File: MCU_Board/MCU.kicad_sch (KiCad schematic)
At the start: 34 parts, among them SW1 SW_SPDT, SW2 SW_Push, U2 STM32L433CCTx, Y1 8MHz, Y2 32kHz

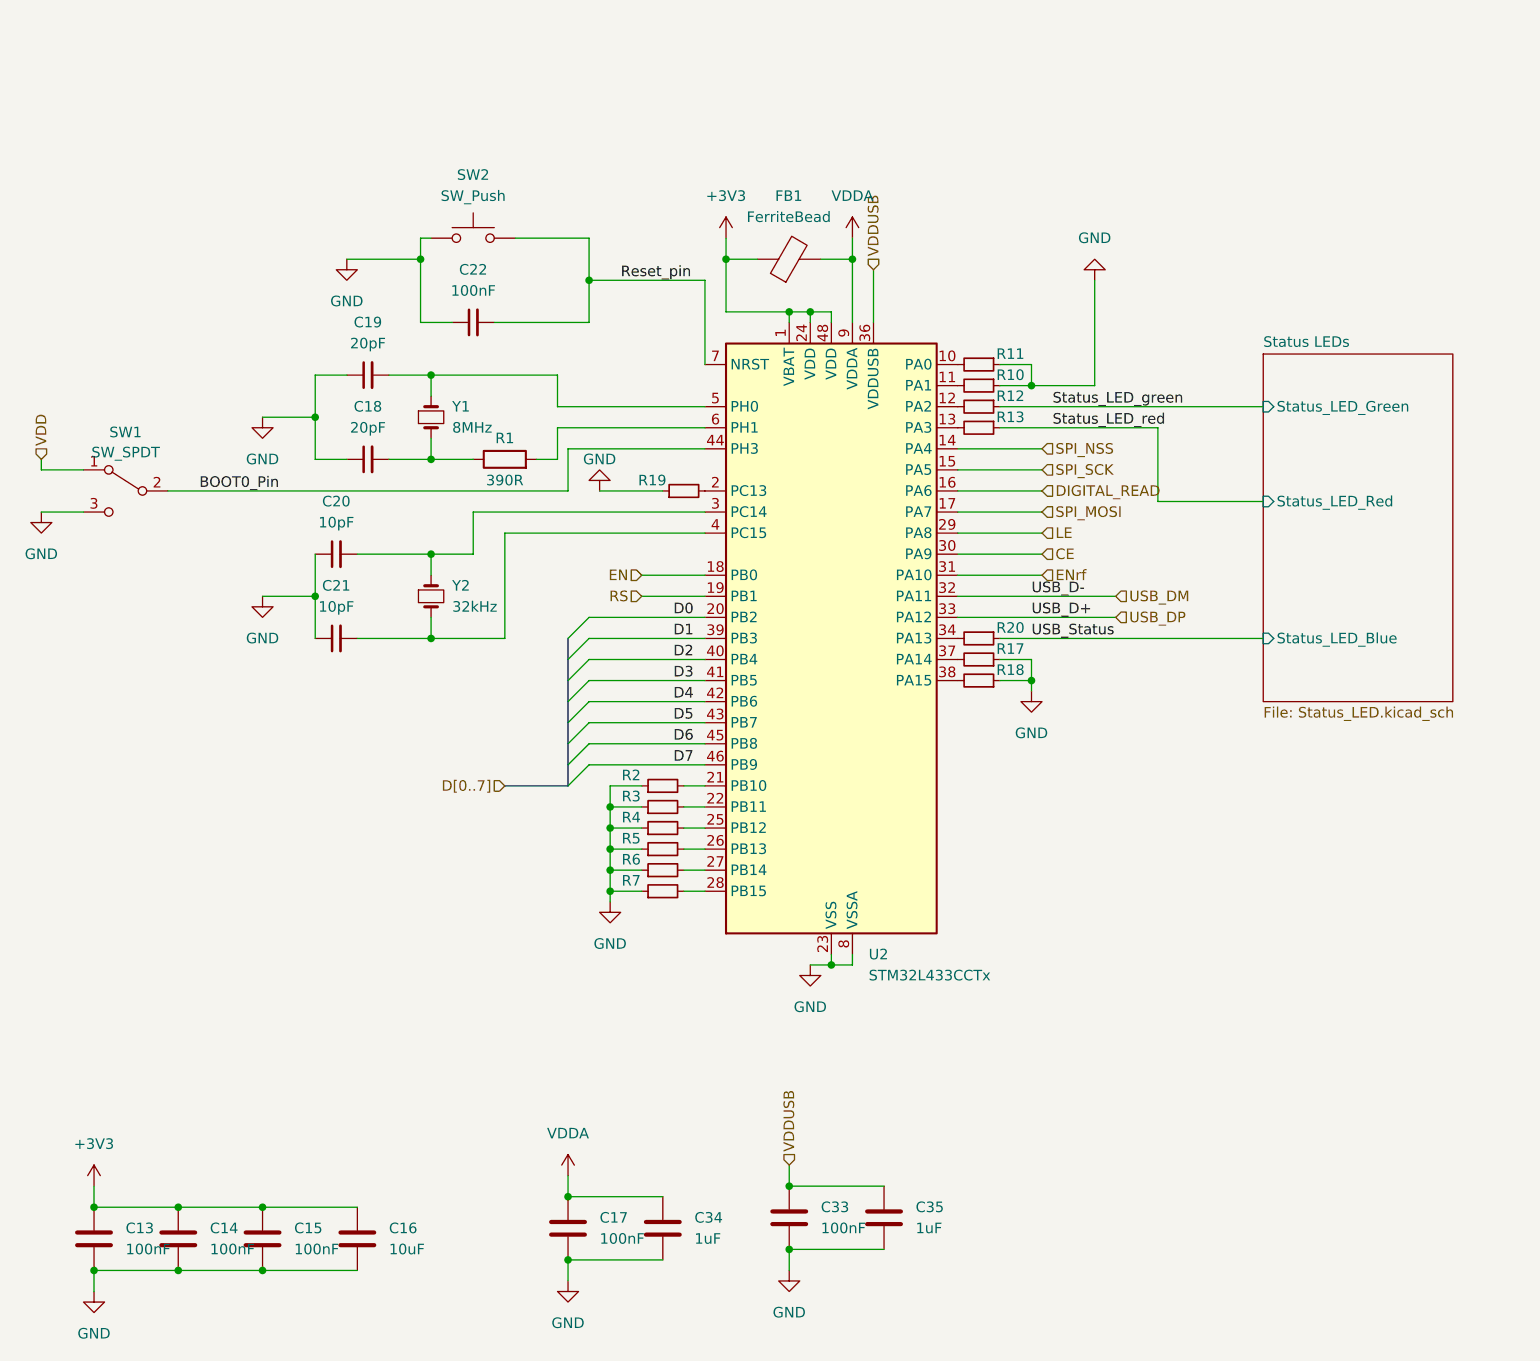
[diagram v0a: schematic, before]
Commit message: Added JTAG connector to MCU board
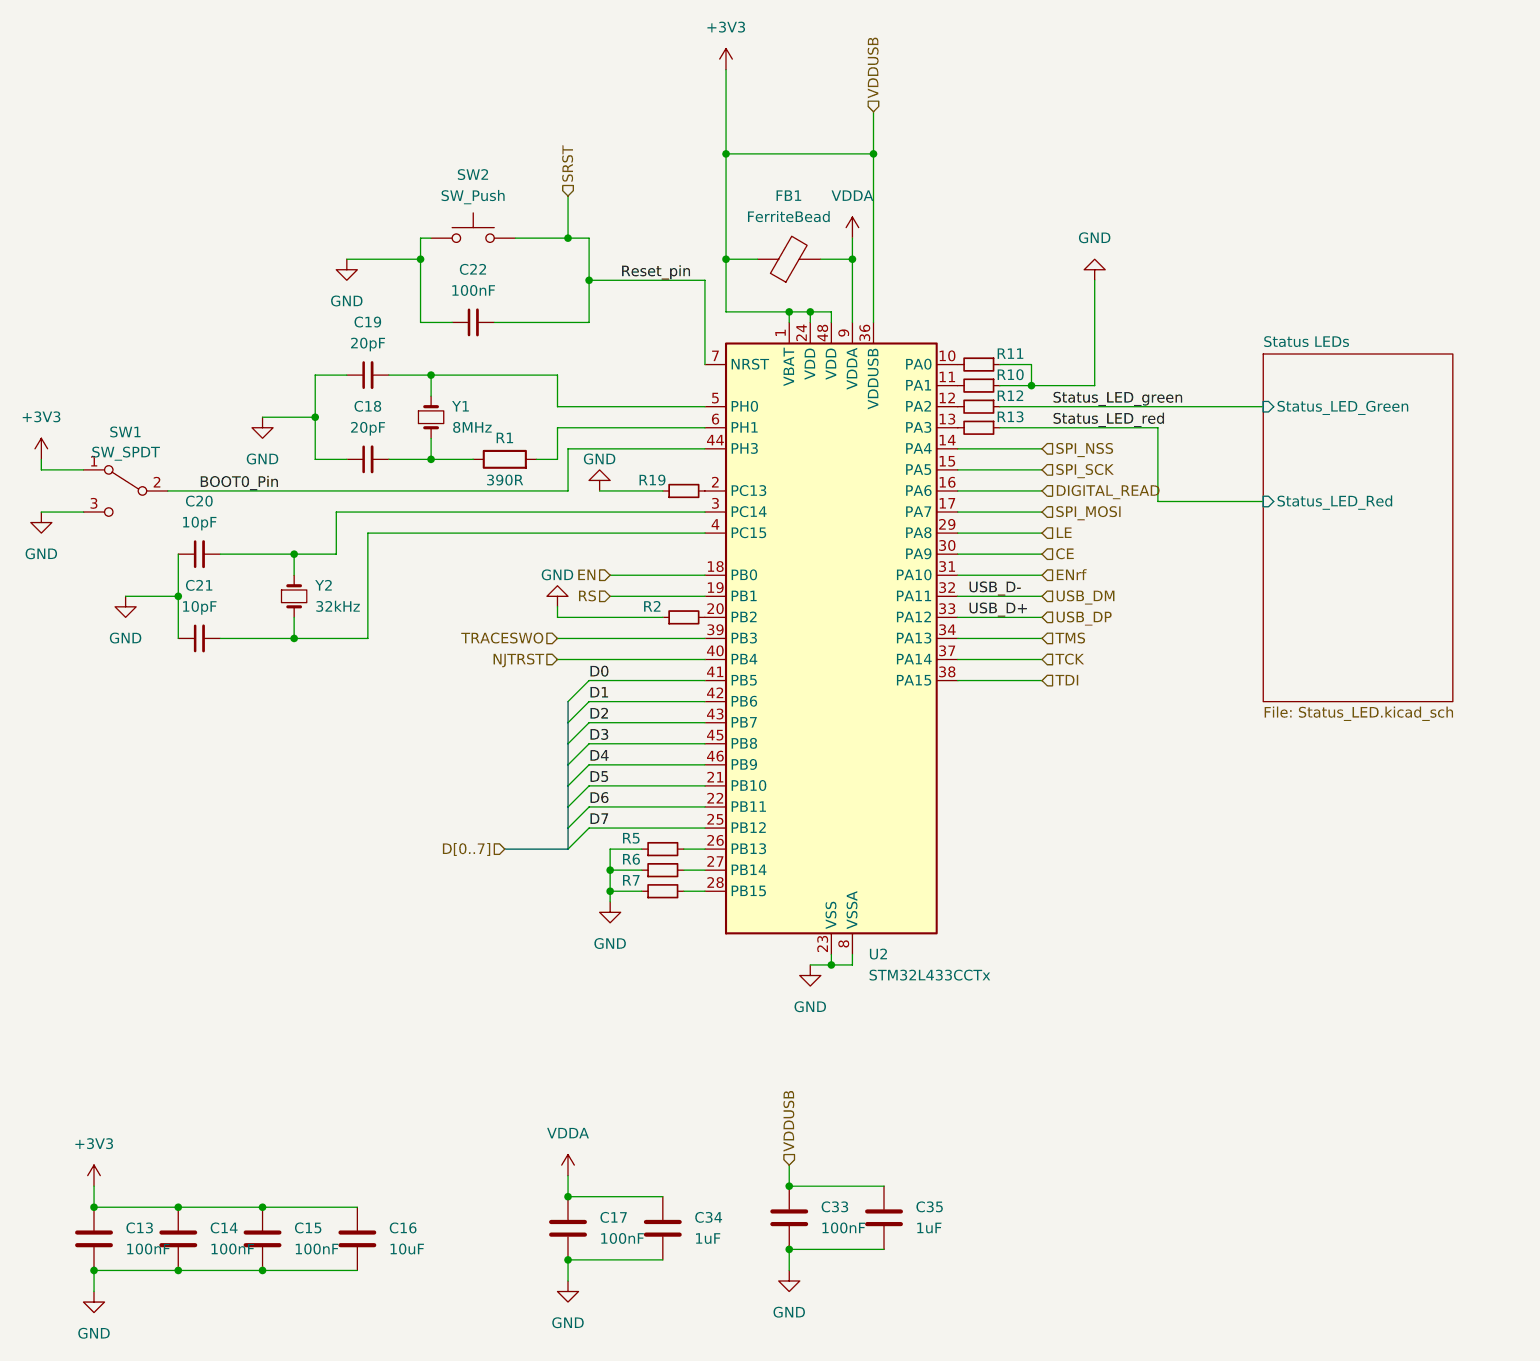
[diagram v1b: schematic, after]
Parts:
- removed R17, R18, R20, R3, R4: 10k, Resistor_SMD:R_0603_1608Metric_Pad0.98x0.95mm_HandSolder, symbol Device:R_Small
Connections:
- net VDD is gone; now on net +3V3: SW1.1 (A)
- net VDDUSB is gone; now on net +3V3: C33.1, C35.1, U2.36 (VDDUSB)
- net D0: now also U2.41 (PB5); no longer U2.20 (PB2)
- net D1: now also U2.42 (PB6); no longer U2.39 (PB3)
- net D2: now also U2.43 (PB7); no longer U2.40 (PB4)
- net D3: now also U2.45 (PB8); no longer U2.41 (PB5)
- net D4: now also U2.46 (PB9); no longer U2.42 (PB6)
- net D5: now also U2.21 (PB10); no longer U2.43 (PB7)
- net D6: now also U2.22 (PB11); no longer U2.45 (PB8)
- net D7: now also U2.25 (PB12); no longer U2.46 (PB9)
- net TMS: now reaches U2.34 (PA13)
- net TCK: now reaches U2.37 (PA14)
- net at R2.2: now also U2.20 (PB2); no longer U2.21 (PB10)
- net TDI: now reaches U2.38 (PA15)
- net Reset_pin renamed SRST
- new net NJTRST: U2.40 (PB4)
- new net TRACESWO: U2.39 (PB3)
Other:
- sheet Status LEDs ports: added none; removed Status_LED_Blue
- moved on the sheet: C20, C21, Y2

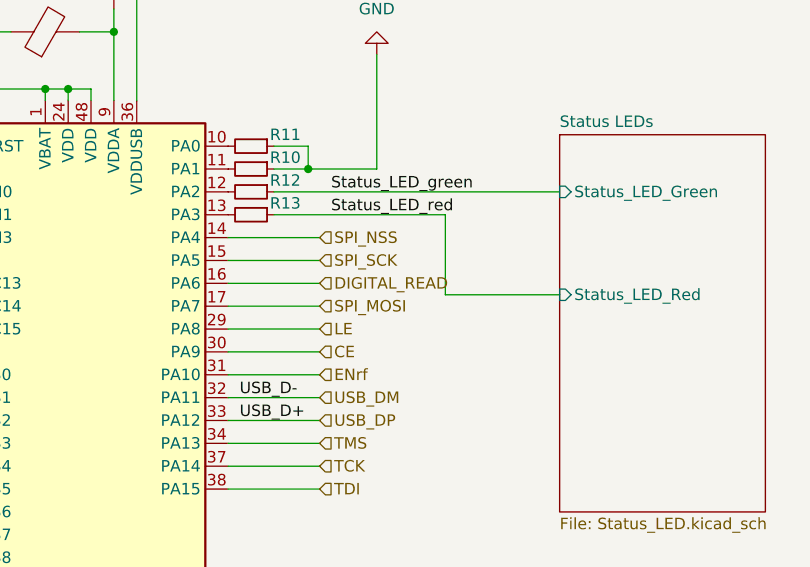
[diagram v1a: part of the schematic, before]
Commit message: Added a header for the VCO controls
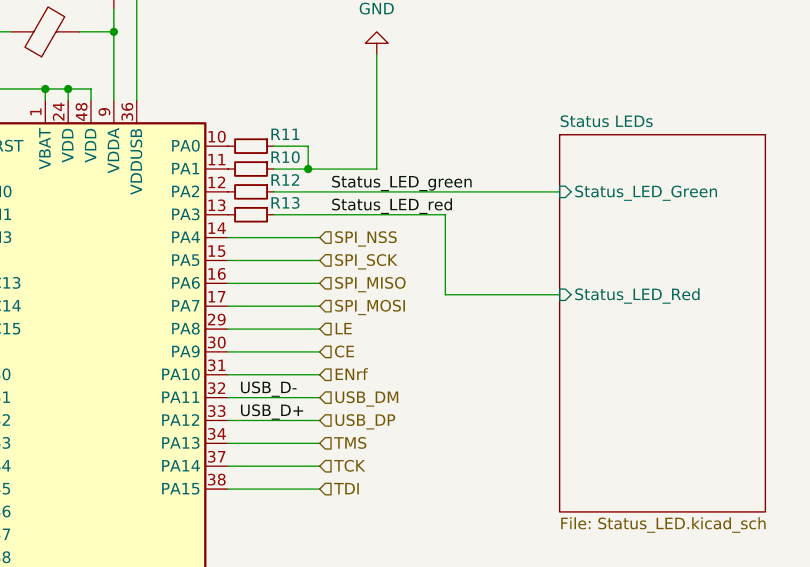
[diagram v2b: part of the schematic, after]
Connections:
- net DIGITAL_READ renamed SPI_MISO
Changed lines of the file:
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@@
     (effects (font (size 1.27 1.27)) (justify left bottom))
   )
-  (hierarchical_label "DIGITAL_READ" (shape input) (at 144.78 78.74 0) (fields_autoplaced)
+  (hierarchical_label "SPI_MISO" (shape input) (at 144.78 78.74 0) (fields_autoplaced)
     (effects (font (size 1.27 1.27)) (justify left))
   )

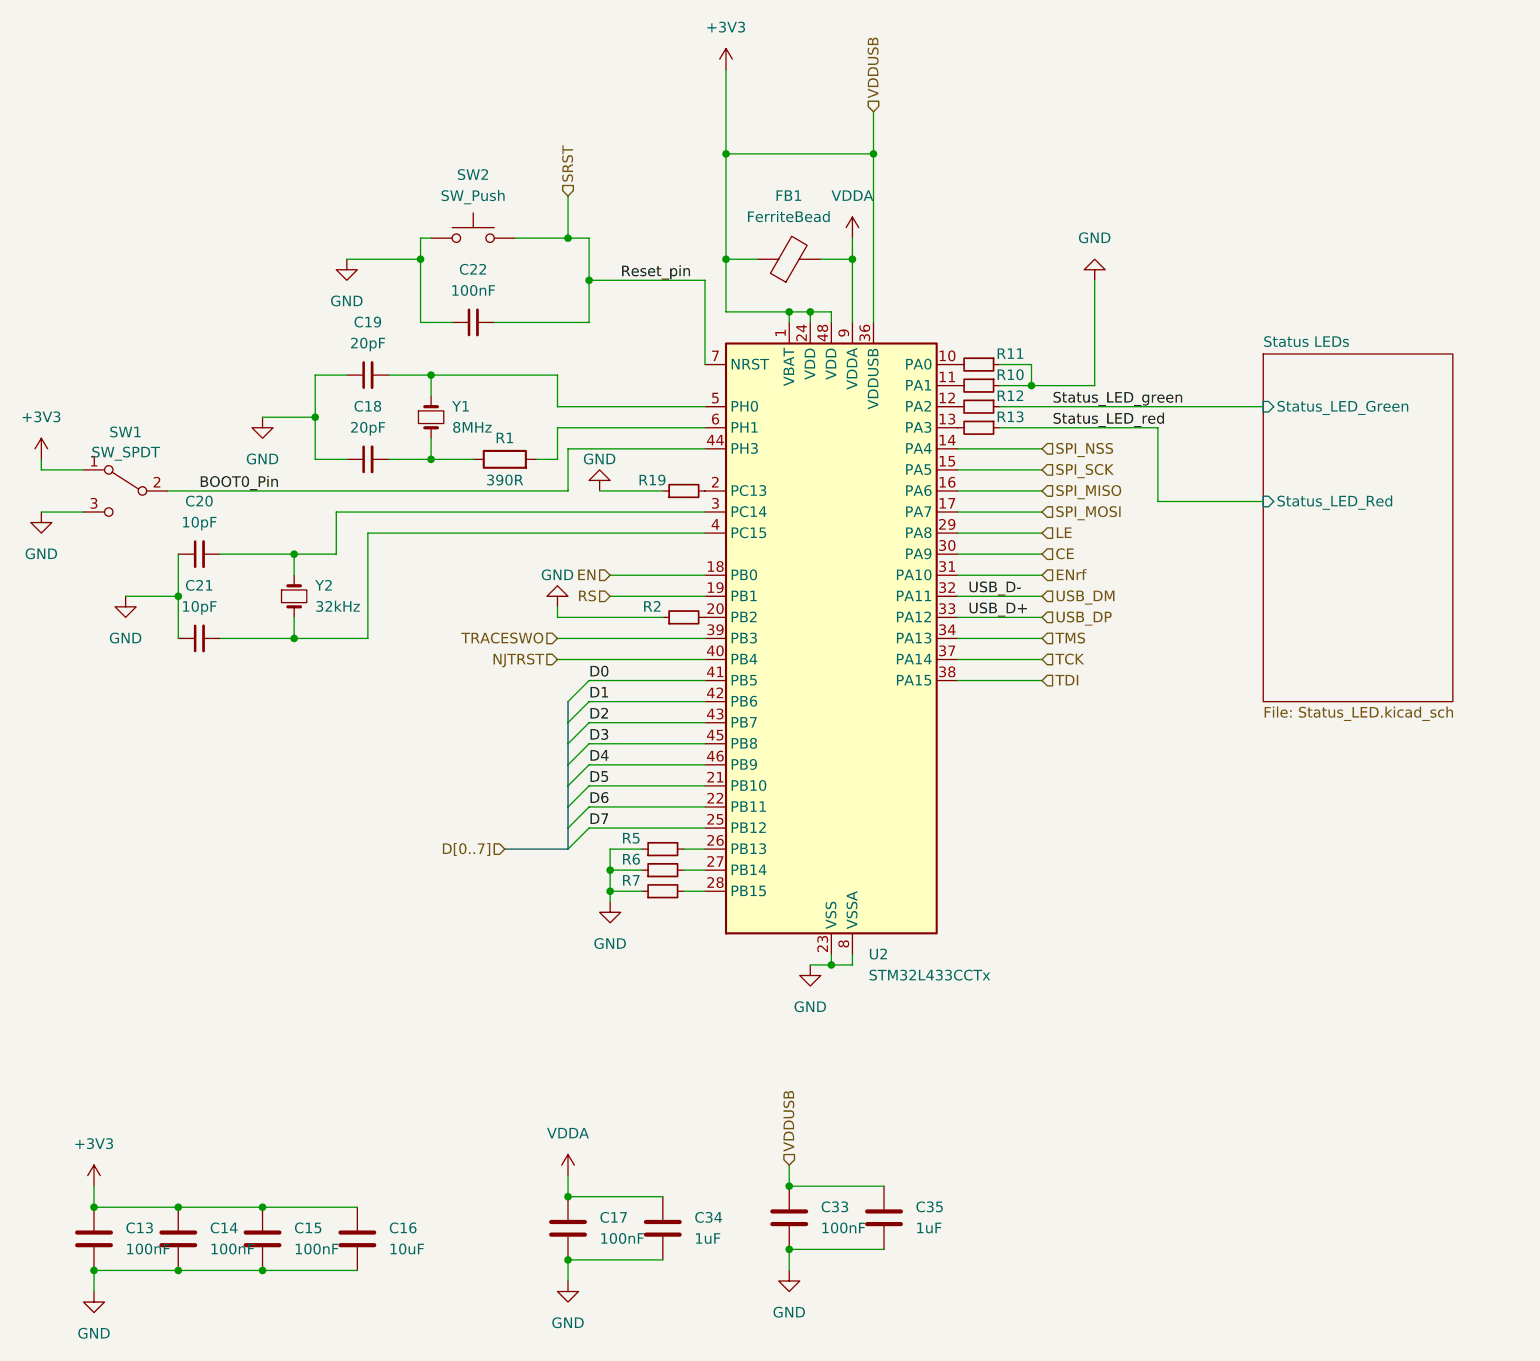
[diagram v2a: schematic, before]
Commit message: Finished MCU board
Finished MCU board and started finishing up the VCO board
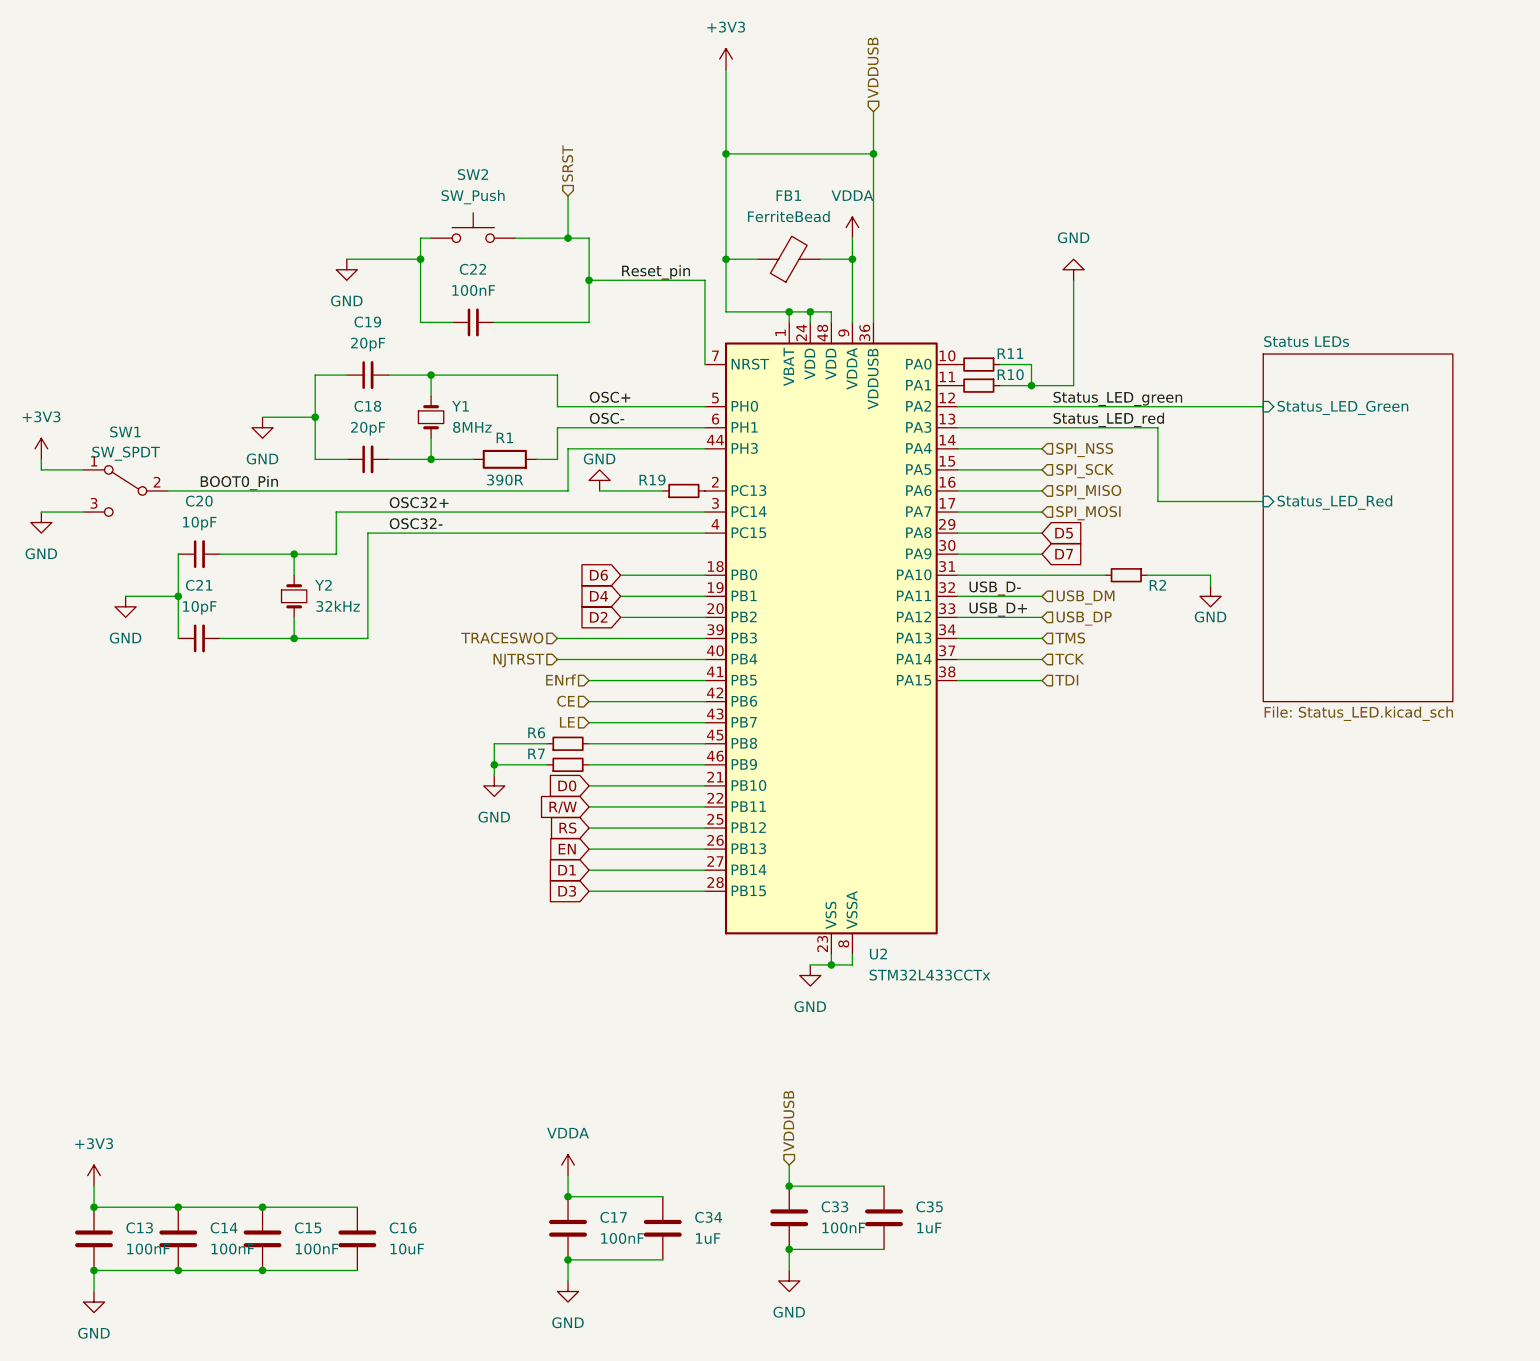
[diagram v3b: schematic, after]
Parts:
- removed R12, R13, R5: 10k, Resistor_SMD:R_0603_1608Metric_Pad0.98x0.95mm_HandSolder, symbol Device:R_Small
- C13, C14, C15, C16, C17, C33, C34, C35: footprint Capacitor_SMD:C_0603_1608Metric_Pad1.08x0.95mm_HandSolder -> Resistor_SMD:R_0402_1005Metric_Pad0.72x0.64mm_HandSolder
- R10, R11, R19, R2, R6, R7: footprint Resistor_SMD:R_0603_1608Metric_Pad0.98x0.95mm_HandSolder -> Resistor_SMD:R_0402_1005Metric_Pad0.72x0.64mm_HandSolder
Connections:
- net CE: now also U2.42 (PB6); no longer U2.30 (PA9)
- net D0: now also U2.21 (PB10); no longer U2.41 (PB5)
- net D1: now also U2.27 (PB14); no longer U2.42 (PB6)
- net D2: now also U2.20 (PB2); no longer U2.43 (PB7)
- net D3: now also U2.28 (PB15); no longer U2.45 (PB8)
- net D4: now also U2.19 (PB1); no longer U2.46 (PB9)
- net D5: now also U2.29 (PA8); no longer U2.21 (PB10)
- net D6: now also U2.18 (PB0); no longer U2.22 (PB11)
- net D7: now also U2.30 (PA9); no longer U2.25 (PB12)
- net EN: now also U2.26 (PB13); no longer U2.18 (PB0)
- net ENrf: now also U2.41 (PB5); no longer U2.31 (PA10)
- net LE: now also U2.43 (PB7); no longer U2.29 (PA8)
- net RS: now also U2.25 (PB12); no longer U2.19 (PB1)
- net Status_LED_green: now also U2.12 (PA2)
- net Status_LED_red: now also U2.13 (PA3)
- net OSC+: now reaches C19.2, U2.5 (PH0), Y1.1
- net OSC32-: now reaches C21.2, U2.4 (PC15), Y2.2
- net at R6.2: now also U2.45 (PB8); no longer U2.27 (PB14)
- net at R7.2: now also U2.46 (PB9); no longer U2.28 (PB15)
- net OSC-: now reaches R1.2, U2.6 (PH1)
- net OSC32+: now reaches C20.2, U2.3 (PC14), Y2.1
- net at R2.2: now also U2.31 (PA10); no longer U2.20 (PB2)
- new net R/W: U2.22 (PB11)
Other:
- moved on the sheet: R2, R6, R7
